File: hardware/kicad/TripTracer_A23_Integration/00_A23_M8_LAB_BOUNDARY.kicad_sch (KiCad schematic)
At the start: 6 parts, among them J901 BENCH ONLY VIN ON PIN1 / UNUS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, J902 M8 3pin VEHICLE (external)

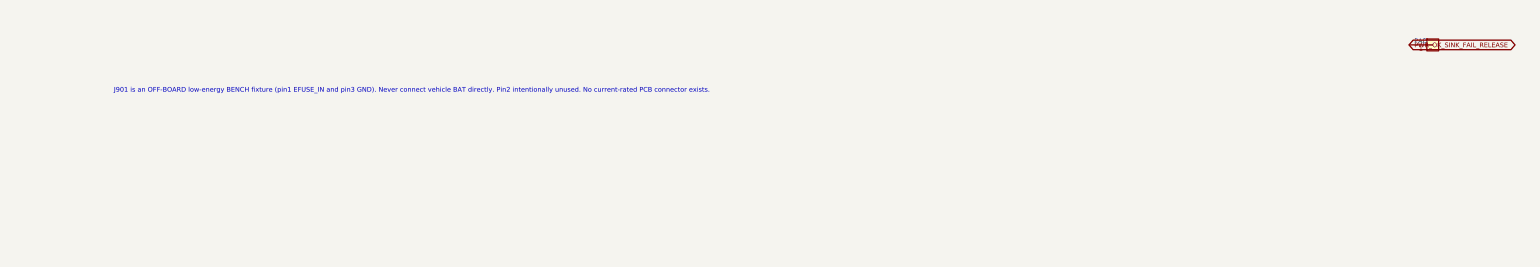
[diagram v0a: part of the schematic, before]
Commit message: TripPower A23 integrated LAB: actually wire host PWR_FAIL 10k AEC-Q200 3V3 pullup to ESP32 GPIO1 and Q501 open drain
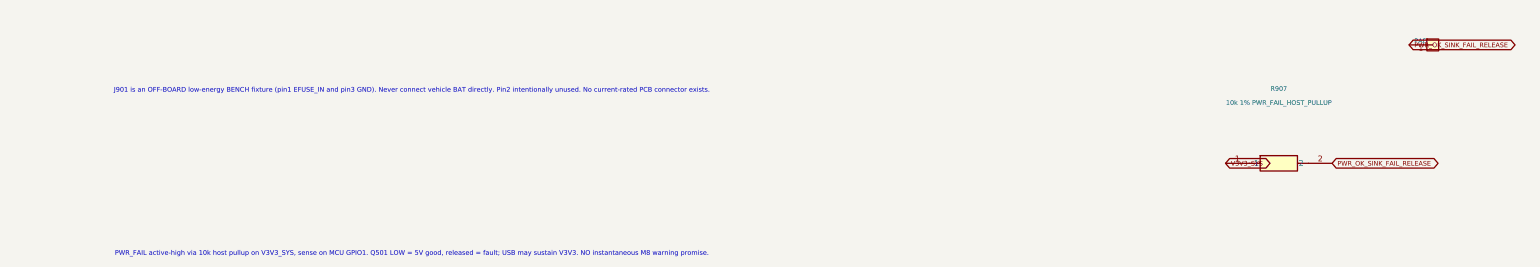
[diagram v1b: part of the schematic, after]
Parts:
- added R907: 10k 1% PWR_FAIL_HOST_PULLUP, Tripmaster:R_1206_3216, symbol Tripmaster_Sym:R
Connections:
- net PWR_OK_SINK_FAIL_RELEASE: now also R907.2
- new net V3V3_SYS: R907.1
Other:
- note added: "PWR_FAIL active-high via 10k host pullup on V3V3_SYS, sense on MCU GPIO1. Q501 LOW = 5V good, released = fault; USB may sustain V3V3. NO instantaneous M8 warning promise."
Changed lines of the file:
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@@
 (instances (project "TripTracer_A23_Integration" (path "/a26d9b0c-7f10-4e5a-a65f-000000000064/a26d9b0c-7f10-4e5a-a65f-000000000070" (reference "TP906") (unit 1)))))
 (global_label "PWR_OK_SINK_FAIL_RELEASE" (shape bidirectional) (at 248.92 170.18 0) (effects (font (size 1 1)) (justify left)))
+(symbol (lib_id "Tripmaster_Sym:R") (at 220.98 195.58 0) (unit 1) (in_bom yes) (on_board yes) (dnp no)
+(property "Reference" "R907" (at 220.98 179.58 0) (effects (font (size 1 1))))
+(property "Value" "10k 1% PWR_FAIL_HOST_PULLUP" (at 220.98 182.58 0) (effects (font (size 1 1))))
+(property "Footprint" "Tripmaster:R_1206_3216" (at 220.98 195.58 0) (effects (font (size 1 1)) (hide yes)))
+(property "MPN" "AC1206FR-0710KL" (at 0 0 0) (effects (font (size 1 1)) (hide yes)))
+(pin "1") (pin "2")
+(instances (project "TripTracer_A23_Integration" (path "/a26d9b0c-7f10-4e5a-a65f-000000000064/a26d9b0c-7f10-4e5a-a65f-000000000070" (reference "R907") (unit 1)))))
+(global_label "V3V3_SYS" (shape bidirectional) (at 209.55 195.58 0) (effects (font (size 1 1)) (justify left)))
+(global_label "PWR_OK_SINK_FAIL_RELEASE" (shape bidirectional) (at 232.41 195.58 0) (effects (font (size 1 1)) (justify left)))
+(text "PWR_FAIL active-high via 10k host pullup on V3V3_SYS, sense on MCU GPIO1. Q501 LOW = 5V good, released = fault; USB may sustain V3V3. NO instantaneous M8 warning promise." (at 35 215 0) (effects (font (size 1.016 1.016))))
 (embedded_fonts no)
 )
